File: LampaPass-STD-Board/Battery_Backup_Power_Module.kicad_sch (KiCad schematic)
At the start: 29 parts, among them J1 Barrel_Jack_Switch, J2 Batt_conn, J3 Termistor, Q1 FDS6898A, Q2 Q_PMOS_GDS, U1 AP9101CK6, U2 MCP73841-410I/UN, U3 TPS2120YFPR

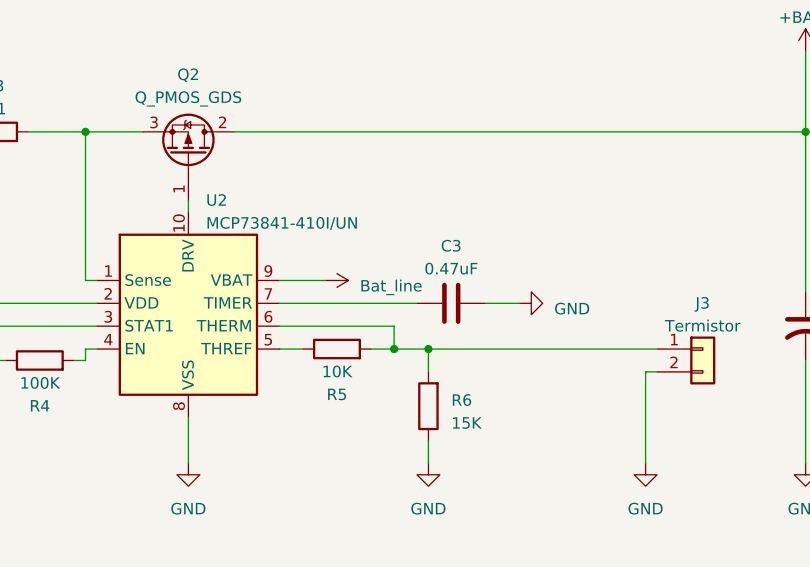
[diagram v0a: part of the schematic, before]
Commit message: Added Battery Backup Power Module. Added Power Mangement empty schematic.
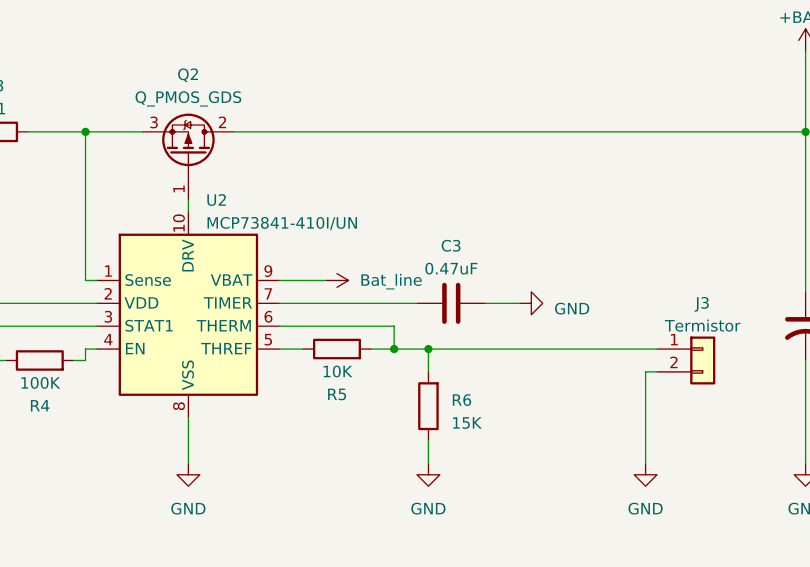
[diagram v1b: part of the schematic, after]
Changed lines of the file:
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@@
       (effects (font (size 1.27 1.27)) hide)
     )
-    (property "Value" "Bat_line" (at 213.36 132.715 90)
+    (property "Value" "Bat_line" (at 213.36 132.08 90)
       (effects (font (size 1.27 1.27)) (justify left))
     )

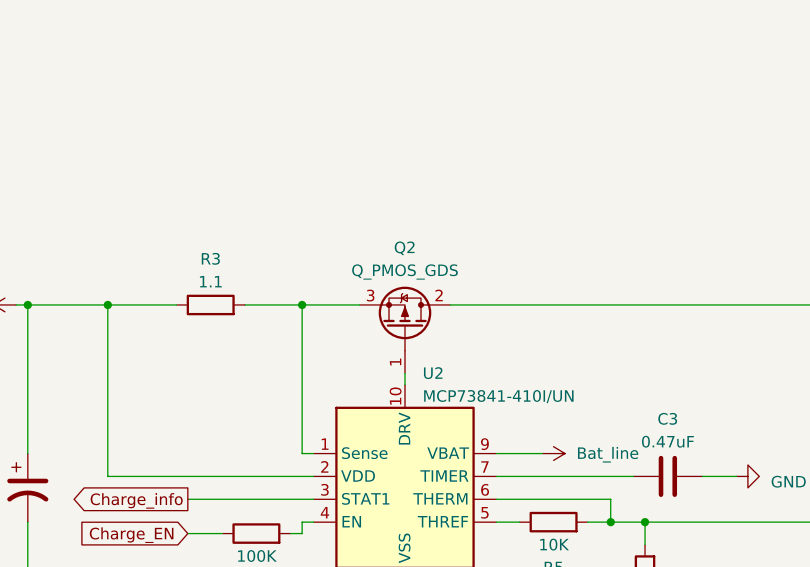
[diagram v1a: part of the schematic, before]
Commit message: Selected connectors and transistors, added footprints for them.
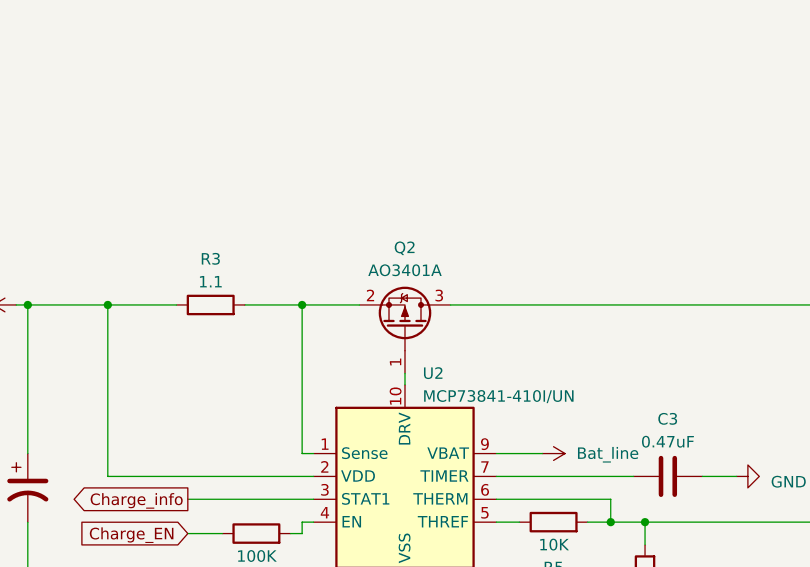
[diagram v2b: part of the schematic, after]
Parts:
- D1: footprint (none) -> Diode_SMD:D_SOD-923; PartNamber (none) -> DF2S6.8FS,L3M
- J1: footprint (none) -> Connector_BarrelJack:BarrelJack_Kycon_KLDX-0202-xC_Horizontal; PartNamber (none) -> KLS1-DC-005A-2.5
- J2: footprint (none) -> Connector_JST:JST_EH_B2B-EH-A_1x02_P2.50mm_Vertical; PartNamber (none) -> B2B-XH-AM(LF)(SN) JST
- J3: footprint (none) -> Connector_PinHeader_2.54mm:PinHeader_1x02_P2.54mm_Vertical; PartNamber (none) -> PLS-2
- Q2: value Q_PMOS_GDS -> AO3401A; footprint (none) -> Package_TO_SOT_SMD:SOT-23-3; symbol Device:Q_PMOS_GDS -> Device:Q_PMOS_GSD; PartNamber (none) -> AO3401A
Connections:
- net +BATT: now also Q2.3 (D); no longer Q2.2 (D)
- net at R3.2, U2.1 (Sense): now also Q2.2 (S); no longer Q2.3 (S)
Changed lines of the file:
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@@
       (effects (font (size 1.27 1.27)))
     )
-    (property "Footprint" "" (at 251.46 139.7 0)
+    (property "Footprint" "Connector_PinHeader_2.54mm:PinHeader_1x02_P2.54mm_Vertical" (at 251.46 139.7 0)
       (effects (font (size 1.27 1.27)) hide)
     )
@@
     )
     (property "Коментарий" "Для https://www.digikey.com/en/products/detail/murata-electronics/NXFT15XV103FEAB050/13904947" (at 251.46 139.7 0)
+      (effects (font (size 1.27 1.27)) hide)
+    )
+    (property "PartNamber" "PLS-2 " (at 251.46 139.7 0)
       (effects (font (size 1.27 1.27)) hide)
     )
@@
       (effects (font (size 1.27 1.27)))
     )
-    (property "Footprint" "" (at 63.5 34.036 0)
+    (property "Footprint" "Connector_BarrelJack:BarrelJack_Kycon_KLDX-0202-xC_Horizontal" (at 63.5 34.036 0)
       (effects (font (size 1.27 1.27)) hide)
     )
@@
       (effects (font (size 1.27 1.27)) hide)
     )
+    (property "PartNamber" "KLS1-DC-005A-2.5" (at 62.23 33.02 0)
+      (effects (font (size 1.27 1.27)) hide)
+    )
     (pin "1")
     (pin "2")
@@
       (effects (font (size 1.27 1.27)) (justify left))
     )
-    (property "Footprint" "" (at 113.03 36.83 0)
+    (property "Footprint" "Diode_SMD:D_SOD-923" (at 113.03 36.83 0)
       (effects (font (size 1.27 1.27)) hide)
     )
     (property "Datasheet" "~" (at 113.03 36.83 0)
+      (effects (font (size 1.27 1.27)) hide)
+    )
+    (property "PartNamber" "DF2S6.8FS,L3M" (at 113.03 36.83 90)
       (effects (font (size 1.27 1.27)) hide)
     )
@@
       (effects (font (size 1.27 1.27)))
     )
-    (property "Footprint" "" (at 34.29 127 0)
+    (property "Footprint" "Connector_JST:JST_EH_B2B-EH-A_1x02_P2.50mm_Vertical" (at 34.29 127 0)
       (effects (font (size 1.27 1.27)) hide)
     )
     (property "Datasheet" "~" (at 34.29 127 0)
+      (effects (font (size 1.27 1.27)) hide)
+    )
+    (property "PartNamber" "B2B-XH-AM(LF)(SN) JST" (at 34.29 127 0)
       (effects (font (size 1.27 1.27)) hide)
     )
@@
     )
   )
-  (symbol (lib_id "Device:Q_PMOS_GDS") (at 194.31 118.11 270) (mirror x) (unit 1)
+  (symbol (lib_id "Device:Q_PMOS_GSD") (at 194.31 118.11 270) (mirror x) (unit 1)
     (in_bom yes) (on_board yes) (dnp no) (fields_autoplaced)
     (property "Reference" "Q2" (at 194.31 109.22 90)
       (effects (font (size 1.27 1.27)))
     )
-    (property "Value" "Q_PMOS_GDS" (at 194.31 111.76 90)
-      (effects (font (size 1.27 1.27)))
-    )
-    (property "Footprint" "" (at 196.85 113.03 0)
+    (property "Value" "AO3401A" (at 194.31 111.76 90)
+      (effects (font (size 1.27 1.27)))
+    )
+    (property "Footprint" "Package_TO_SOT_SMD:SOT-23-3" (at 196.85 113.03 0)
       (effects (font (size 1.27 1.27)) hide)
     )
@@
       (effects (font (size 1.27 1.27)) hide)
     )
+    (property "PartNamber" "AO3401A" (at 194.31 118.11 90)
+      (effects (font (size 1.27 1.27)) hide)
+    )
